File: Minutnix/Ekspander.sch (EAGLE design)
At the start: 14 parts, among them X1 FH12-12S-0.5S_THINNER, X6 JST-XH-03-PIN-LONG-PAD

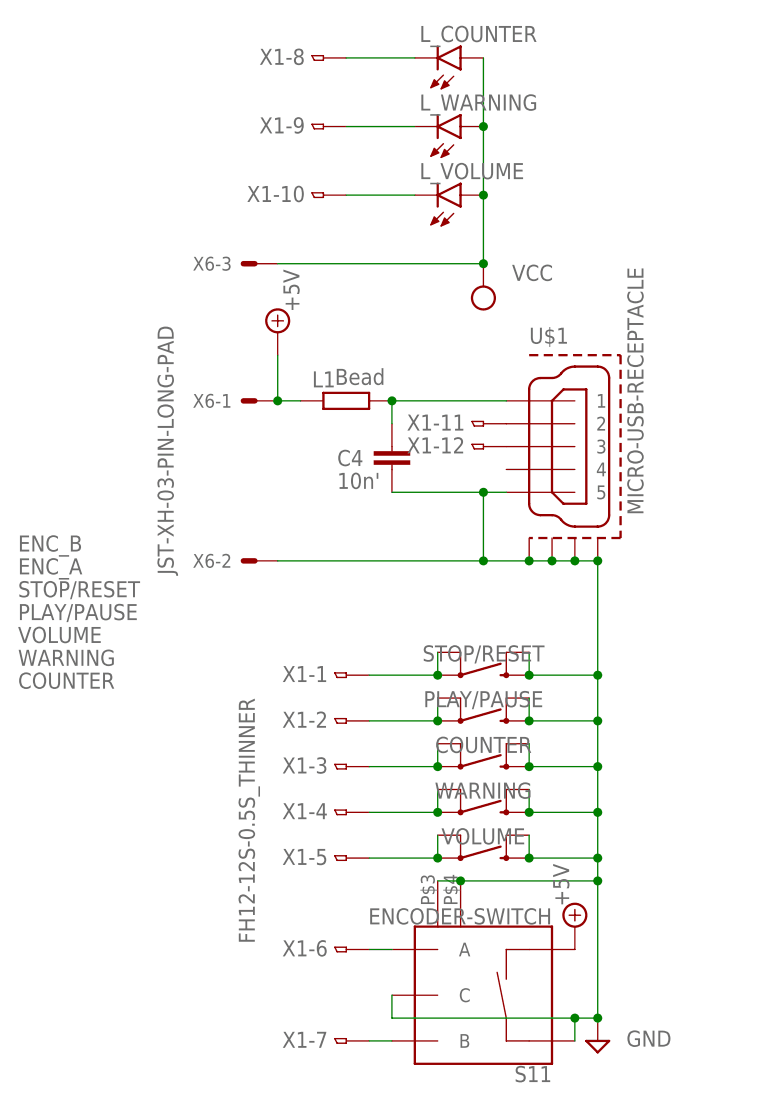
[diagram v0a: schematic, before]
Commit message: rotation of tape ports
also some nets wider
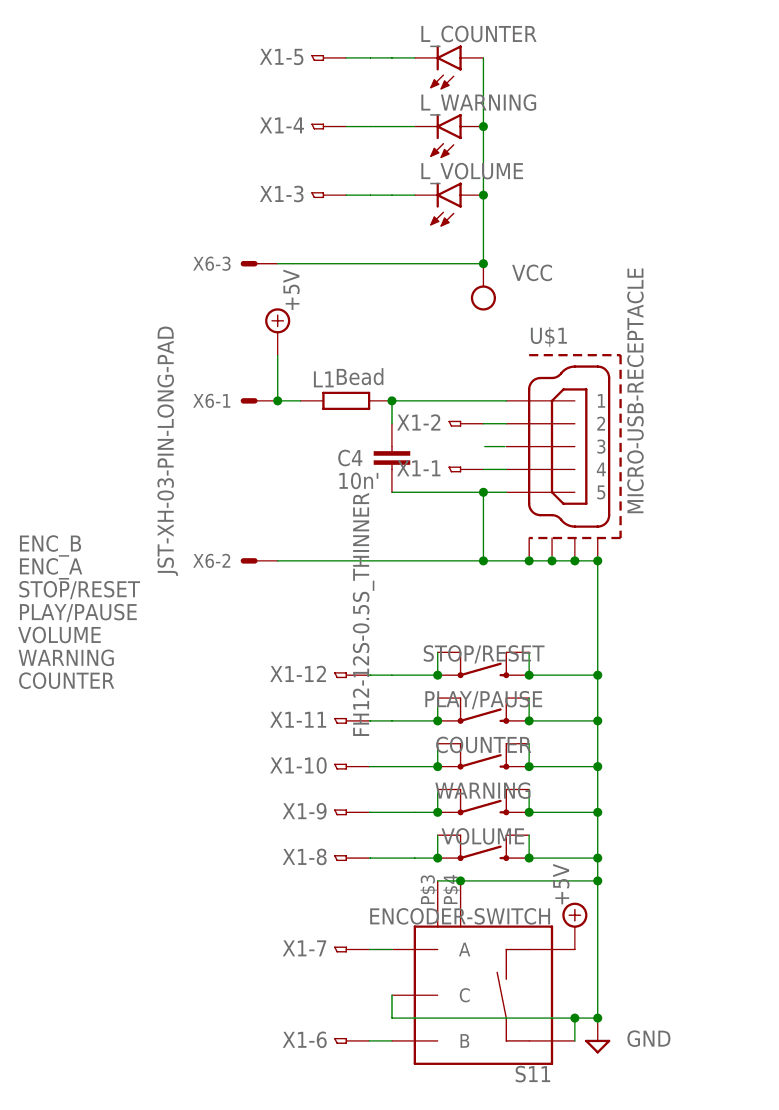
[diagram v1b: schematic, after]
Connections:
- removed net N$8: S11.B, X1-7.1
- removed net N$9: U$1.3, X1-12.1
- new net N$17: U$1.4, X1-1.1
- new net N$18: U$1.2, X1-2.1
- net N$1: now also X1-7.1; no longer X1-6.1
- net N$10: now also X1-5.1; no longer X1-8.1
- net N$11: now also X1-4.1; no longer X1-9.1
- net N$12: now also X1-3.1; no longer X1-10.1
- net N$2: now also X1-12.1; no longer X1-1.1
- net N$3: now also X1-11.1; no longer X1-2.1
- net N$4: now also X1-10.1; no longer X1-3.1
- net N$5: now also X1-9.1; no longer X1-4.1
- net N$6: now also X1-8.1; no longer X1-5.1
- net N$7: now also S11.B, X1-6.1; no longer U$1.2, X1-11.1
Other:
- moved on the sheet: X1-1, X1-10, X1-11, X1-12, X1-2, X1-3, X1-4, X1-5, X1-6, X1-7, X1-8, X1-9

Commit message: expander pools
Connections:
- net GND: now also X1CASE12.1
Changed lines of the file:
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@@
 <grid distance="0.1" unitdist="inch" unit="inch" style="lines" multiple="1" display="no" altdistance="0.01" altunitdist="inch" altunit="inch"/>
 <layers>
-<layer number="1" name="Top" color="4" fill="1" visible="no" active="no"/>
-<layer number="2" name="Route2" color="16" fill="1" visible="no" active="no"/>
-<layer number="3" name="Route3" color="17" fill="1" visible="no" active="no"/>
-<layer number="4" name="Route4" color="18" fill="1" visible="no" active="no"/>
-<layer number="5" name="Route5" color="19" fill="1" visible="no" active="no"/>
-<layer number="6" name="Route6" color="25" fill="1" visible="no" active="no"/>
-<layer number="7" name="Route7" color="26" fill="1" visible="no" active="no"/>
-<layer number="8" name="Route8" color="27" fill="1" visible="no" active="no"/>
-<layer number="9" name="Route9" color="28" fill="1" visible="no" active="no"/>
-<layer number="10" name="Route10" color="29" fill="1" visible="no" active="no"/>
-<layer number="11" name="Route11" color="30" fill="1" visible="no" active="no"/>
-<layer number="12" name="Route12" color="20" fill="1" visible="no" active="no"/>
-<layer number="13" name="Route13" color="21" fill="1" visible="no" active="no"/>
-<layer number="14" name="Route14" color="22" fill="1" visible="no" active="no"/>
-<layer number="15" name="Route15" color="23" fill="1" visible="no" active="no"/>
-<layer number="16" name="Bottom" color="1" fill="1" visible="no" active="no"/>
-<layer number="17" name="Pads" color="2" fill="1" visible="no" active="no"/>
-<layer number="18" name="Vias" color="2" fill="1" visible="no" active="no"/>
-<layer number="19" name="Unrouted" color="6" fill="1" visible="no" active="no"/>
-<layer number="20" name="Dimension" color="24" fill="1" visible="no" active="no"/>
-<layer number="21" name="tPlace" color="7" fill="1" visible="no" active="no"/>
-<layer number="22" name="bPlace" color="7" fill="1" visible="no" active="no"/>
-<layer number="23" name="tOrigins" color="15" fill="1" visible="no" active="no"/>
-<layer number="24" name="bOrigins" color="15" fill="1" visible="no" active="no"/>
-<layer number="25" name="tNames" color="7" fill="1" visible="no" active="no"/>
-<layer number="26" name="bNames" color="7" fill="1" visible="no" active="no"/>
-<layer number="27" name="tValues" color="7" fill="1" visible="no" active="no"/>
-<layer number="28" name="bValues" color="7" fill="1" visible="no" active="no"/>
+<layer number="1" name="Top" color="4" fill="1" visible="yes" active="no"/>
+<layer number="2" name="Route2" color="16" fill="1" visible="yes" active="no"/>
+<layer number="3" name="Route3" color="17" fill="1" visible="yes" active="no"/>
+<layer number="4" name="Route4" color="18" fill="1" visible="yes" active="no"/>
+<layer number="5" name="Route5" color="19" fill="1" visible="yes" active="no"/>
+<layer number="6" name="Route6" color="25" fill="1" visible="yes" active="no"/>
+<layer number="7" name="Route7" color="26" fill="1" visible="yes" active="no"/>
+<layer number="8" name="Route8" color="27" fill="1" visible="yes" active="no"/>
+<layer number="9" name="Route9" color="28" fill="1" visible="yes" active="no"/>
+<layer number="10" name="Route10" color="29" fill="1" visible="yes" active="no"/>
+<layer number="11" name="Route11" color="30" fill="1" visible="yes" active="no"/>
+<layer number="12" name="Route12" color="20" fill="1" visible="yes" active="no"/>
+<layer number="13" name="Route13" color="21" fill="1" visible="yes" active="no"/>
+<layer number="14" name="Route14" color="22" fill="1" visible="yes" active="no"/>
+<layer number="15" name="Route15" color="23" fill="1" visible="yes" active="no"/>
+<layer number="16" name="Bottom" color="1" fill="1" visible="yes" active="no"/>
+<layer number="17" name="Pads" color="2" fill="1" visible="yes" active="no"/>
+<layer number="18" name="Vias" color="2" fill="1" visible="yes" active="no"/>
+<layer number="19" name="Unrouted" color="6" fill="1" visible="yes" active="no"/>
+<layer number="20" name="Dimension" color="24" fill="1" visible="yes" active="no"/>
+<layer number="21" name="tPlace" color="7" fill="1" visible="yes" active="no"/>
+<layer number="22" name="bPlace" color="7" fill="1" visible="yes" active="no"/>
+<layer number="23" name="tOrigins" color="15" fill="1" visible="yes" active="no"/>
+<layer number="24" name="bOrigins" color="15" fill="1" visible="yes" active="no"/>
+<layer number="25" name="tNames" color="7" fill="1" visible="yes" active="no"/>
+<layer number="26" name="bNames" color="7" fill="1" visible="yes" active="no"/>
+<layer number="27" name="tValues" color="7" fill="1" visible="yes" active="no"/>
+<layer number="28" name="bValues" color="7" fill="1" visible="yes" active="no"/>
 <layer number="29" name="tStop" color="7" fill="3" visible="no" active="no"/>
 <layer number="30" name="bStop" color="7" fill="6" visible="no" active="no"/>
@@
 <layer number="35" name="tGlue" color="7" fill="4" visible="no" active="no"/>
 <layer number="36" name="bGlue" color="7" fill="5" visible="no" active="no"/>
-<layer number="37" name="tTest" color="7" fill="1" visible="no" active="no"/>
-<layer number="38" name="bTest" color="7" fill="1" visible="no" active="no"/>
+<layer number="37" name="tTest" color="7" fill="1" visible="yes" active="no"/>
+<layer number="38" name="bTest" color="7" fill="1" visible="yes" active="no"/>
 <layer number="39" name="tKeepout" color="4" fill="11" visible="no" active="no"/>
 <layer number="40" name="bKeepout" color="1" fill="11" visible="no" active="no"/>
@@
 <layer number="44" name="Drills" color="7" fill="1" visible="no" active="no"/>
 <layer number="45" name="Holes" color="7" fill="1" visible="no" active="no"/>
-<layer number="46" name="Milling" color="3" fill="1" visible="no" active="no"/>
-<layer number="47" name="Measures" color="7" fill="1" visible="no" active="no"/>
-<layer number="48" name="Document" color="7" fill="1" visible="no" active="no"/>
-<layer number="49" name="Reference" color="7" fill="1" visible="no" active="no"/>
-<layer number="50" name="dxf" color="7" fill="1" visible="no" active="no"/>
-<layer number="51" name="tDocu" color="7" fill="1" visible="no" active="no"/>
-<layer number="52" name="bDocu" color="7" fill="1" visible="no" active="no"/>
-<layer number="53" name="tGND_GNDA" color="7" fill="9" visible="no" active="no"/>
-<layer number="54" name="bGND_GNDA" color="1" fill="9" visible="no" active="no"/>
-<layer number="56" name="wert" color="7" fill="1" visible="no" active="no"/>
-<layer number="57" name="tCAD" color="7" fill="1" visible="no" active="no"/>
-<layer number="59" name="tCarbon" color="7" fill="1" visible="no" active="no"/>
-<layer number="60" name="bCarbon" color="7" fill="1" visible="no" active="no"/>
+<layer number="46" name="Milling" color="3" fill="1" visible="yes" active="no"/>
+<layer number="47" name="Measures" color="7" fill="1" visible="yes" active="no"/>
+<layer number="48" name="Document" color="7" fill="1" visible="yes" active="no"/>
+<layer number="49" name="Reference" color="7" fill="1" visible="yes" active="no"/>
+<layer number="50" name="dxf" color="7" fill="1" visible="yes" active="no"/>
+<layer number="51" name="tDocu" color="7" fill="1" visible="yes" active="no"/>
+<layer number="52" name="bDocu" color="7" fill="1" visible="yes" active="no"/>
+<layer number="53" name="tGND_GNDA" color="7" fill="9" visible="yes" active="no"/>
+<layer number="54" name="bGND_GNDA" color="1" fill="9" visible="yes" active="no"/>
+<layer number="56" name="wert" color="7" fill="1" visible="yes" active="no"/>
+<layer number="57" name="tCAD" color="7" fill="1" visible="yes" active="no"/>
+<layer number="59" name="tCarbon" color="7" fill="1" visible="yes" active="no"/>
+<layer number="60" name="bCarbon" color="7" fill="1" visible="yes" active="no"/>
 <layer number="88" name="SimResults" color="9" fill="1" visible="yes" active="yes"/>
 <layer number="89" name="SimProbes" color="9" fill="1" visible="yes" active="yes"/>
@@
 <attribute name="VALUE" x="90.805" y="116.205" size="1.778" layer="96" rot="MR270"/>
 </instance>
+<instance part="X1" gate="CASE12" x="96.52" y="101.6" smashed="yes">
+<attribute name="NAME" x="98.552" y="100.838" size="1.778" layer="95"/>
+</instance>
 </instances>
 <busses>
@@
 <wire x1="93.98" y1="121.92" x2="93.98" y2="116.84" width="0.1524" layer="91"/>
 <wire x1="93.98" y1="116.84" x2="93.98" y2="114.3" width="0.1524" layer="91"/>
-<wire x1="93.98" y1="114.3" x2="93.98" y2="99.06" width="0.1524" layer="91"/>
+<wire x1="93.98" y1="114.3" x2="93.98" y2="101.6" width="0.1524" layer="91"/>
+<wire x1="93.98" y1="101.6" x2="93.98" y2="99.06" width="0.1524" layer="91"/>
 <wire x1="71.12" y1="99.06" x2="91.44" y2="99.06" width="0.1524" layer="91"/>
 <pinref part="S11" gate="G$1" pin="C"/>
@@
 <wire x1="91.44" y1="96.52" x2="91.44" y2="99.06" width="0.1524" layer="91"/>
 <junction x="91.44" y="99.06"/>
-</segment>
-</net>
+<pinref part="X1" gate="CASE12" pin="1"/>
+<junction x="93.98" y="101.6"/>
+</segment>
+</net>

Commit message: Many final changes
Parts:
- removed X1: FH12-12S-0.5S_THINNER, My_con-hirose:FH12-12S-0.5S_THINNER
- added FFC_CON: FH12-12S-0.5S_THINNER, My_con-hirose:FH12-12S-0.5S_THINNER
- added JP1: (no value), pinhead:PINHD-1X1
- renumbered S11 to ENCODER, X6 to POWER_CON
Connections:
- removed net N$1: ENCODER.A, X1-7.1
- removed net N$10: L_COUNTER.C, X1-5.1
- removed net N$11: L_WARNING.C, X1-4.1
- removed net N$12: L_VOLUME.C, X1-3.1
- removed net N$17: U$1.4, X1-1.1
- removed net N$18: U$1.2, X1-2.1
- removed net N$2: STOP/RESET.1, STOP/RESET.3, X1-12.1
- removed net N$3: PLAY/PAUSE.1, PLAY/PAUSE.3, X1-11.1
- removed net N$4: COUNTER.1, COUNTER.3, X1-10.1
- removed net N$5: WARNING.1, WARNING.3, X1-9.1
- removed net N$6: VOLUME.1, VOLUME.3, X1-8.1
- removed net N$7: ENCODER.B, X1-6.1
- new net COUNTER: COUNTER.1, COUNTER.3, FFC_CON-5.1
- new net DM: FFC_CON-11.1, U$1.2
- new net DP: FFC_CON-12.1, U$1.3
- new net ENC_A: ENCODER.A, FFC_CON-6.1
- new net ENC_B: ENCODER.B, FFC_CON-7.1
- new net L_COUNTER: FFC_CON-8.1, L_COUNTER.C
- new net L_VOLUME: FFC_CON-10.1, L_VOLUME.C
- new net L_WARNING: FFC_CON-9.1, L_WARNING.C
- new net N$8: JP1.1, U$1.4
- new net PLAY/PAUSE: FFC_CON-1.1, PLAY/PAUSE.1, PLAY/PAUSE.3
- new net STOP/RESET: FFC_CON-2.1, STOP/RESET.1, STOP/RESET.3
- new net VOLUME: FFC_CON-3.1, VOLUME.1, VOLUME.3
- new net WARNING: FFC_CON-4.1, WARNING.1, WARNING.3
- net +5V: now also ENCODER.GND1; no longer ENCODER.SW-
- net GND: no longer ENCODER.GND1, ENCODER.GND2, ENCODER.SW+, X1CASE12.1
